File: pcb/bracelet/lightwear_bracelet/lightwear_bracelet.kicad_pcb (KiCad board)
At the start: 2 copper layers, 31 x 20 mm, 20 parts, among them Q1 NMOS, SW1 SW_SPST, U1 ATtiny1616-M, U2 TP4054

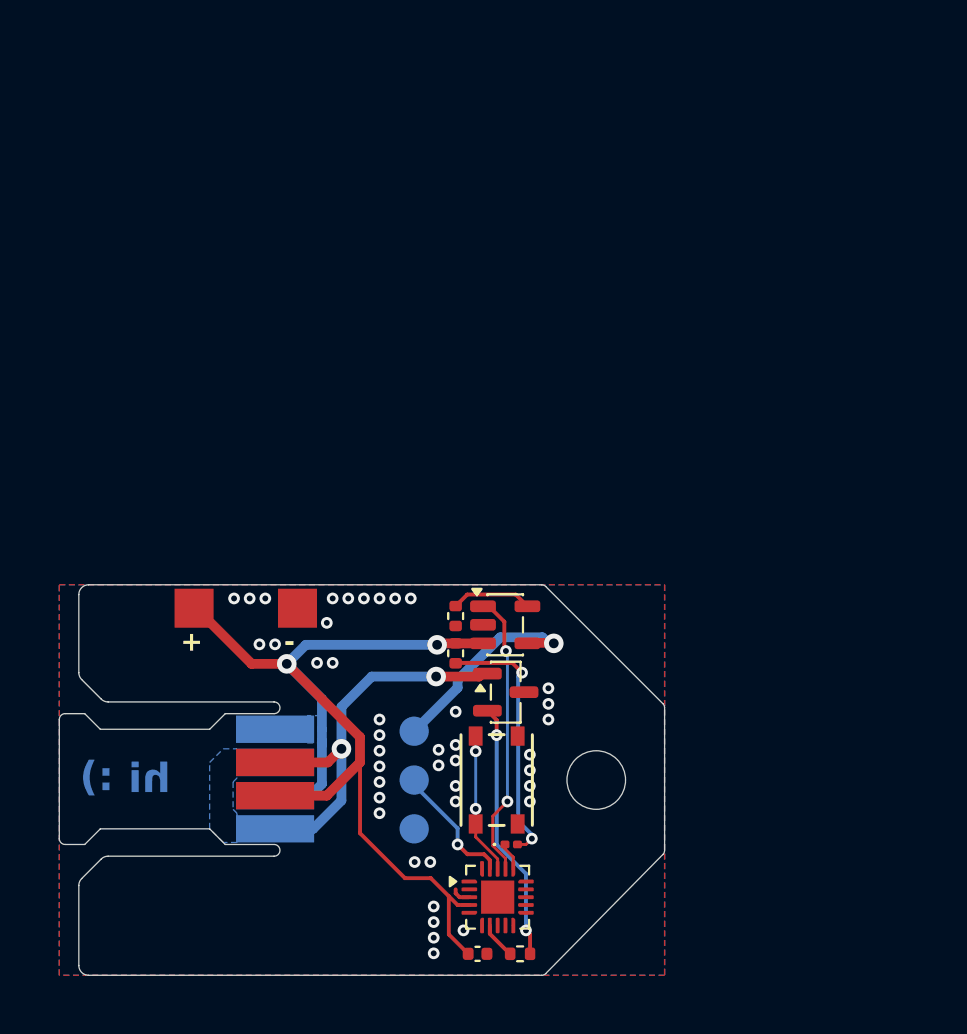
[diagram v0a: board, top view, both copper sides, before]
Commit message: Started work on PCB without battery chips
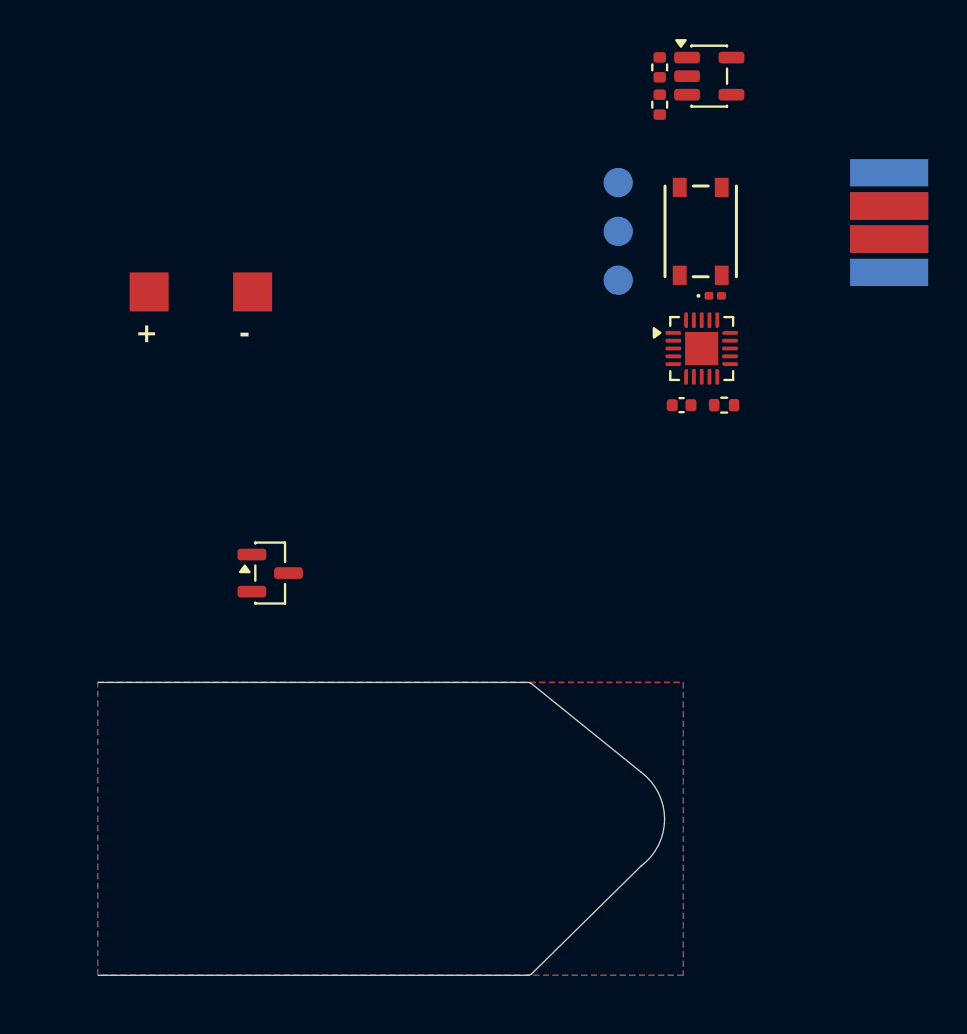
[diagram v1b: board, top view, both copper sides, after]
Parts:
- moved TP10 42.4 mm to (170.5, 58.9)
- moved TP5 42.4 mm to (170.5, 62.3)
- moved TP8 42.4 mm to (170.5, 62.3)
- moved TP9 42.4 mm to (170.5, 64.0)
- moved TP11 42.4 mm to (170.5, 60.6)
- moved TP4 42.4 mm to (170.5, 60.6)
- moved C1 30.0 mm to (159.9, 70.8)
- moved R3 30.0 mm to (162.1, 70.8)
- moved D1 30.0 mm to (161.6, 65.2)
- moved R1 30.0 mm to (158.8, 55.4)
- moved U1 30.0 mm to (160.9, 67.9)
- moved SW1 30.0 mm to (160.8, 61.9)
- moved TP1 30.0 mm to (156.6, 59.4)
- moved TP2 30.0 mm to (156.6, 61.9)
- moved R2 30.0 mm to (158.8, 53.5)
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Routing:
- net +BATT: track 51.7 -> 0.00 mm, vias 2 -> 0
- net /LEDK: track 20.3 -> 0.00 mm, vias 2 -> 0
- net /nCHRG: track 14.9 -> 0.00 mm, vias 2 -> 0
- net Net-(Q1-G): track 13.8 -> 0.00 mm, vias 2 -> 0
- net Net-(D1-A): track 13.5 -> 0.00 mm, vias 2 -> 0
- net +5V: track 10.9 -> 0.00 mm, vias 1 -> 0
- net Net-(SW1-A): track 7.27 -> 0.00 mm, vias 2 -> 0
- net /UPDI: track 6.65 -> 0.00 mm, vias 1 -> 0
- net Net-(U2-PROG): track 4.17 -> 0.00 mm
- net Net-(U1-PA6): track 1.89 -> 0.00 mm
- net Net-(D1-K): track 1.43 -> 0.00 mm
- net GND: track 0.98 -> 0.00 mm, vias 42 -> 0
- removed copper zone on B.Cu, net +BATT
- removed copper zone on B.Cu, net /LEDK
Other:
- board size 31 x 20 mm -> 29 x 15 mm
- board text removed: ":)"
- board text removed: "Stiffener: Polyimide Thickness: 0.15mm Location: Filled zones on this layer, back side of PCB"
- board text removed: "hi"

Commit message: 15x20mm battery version done
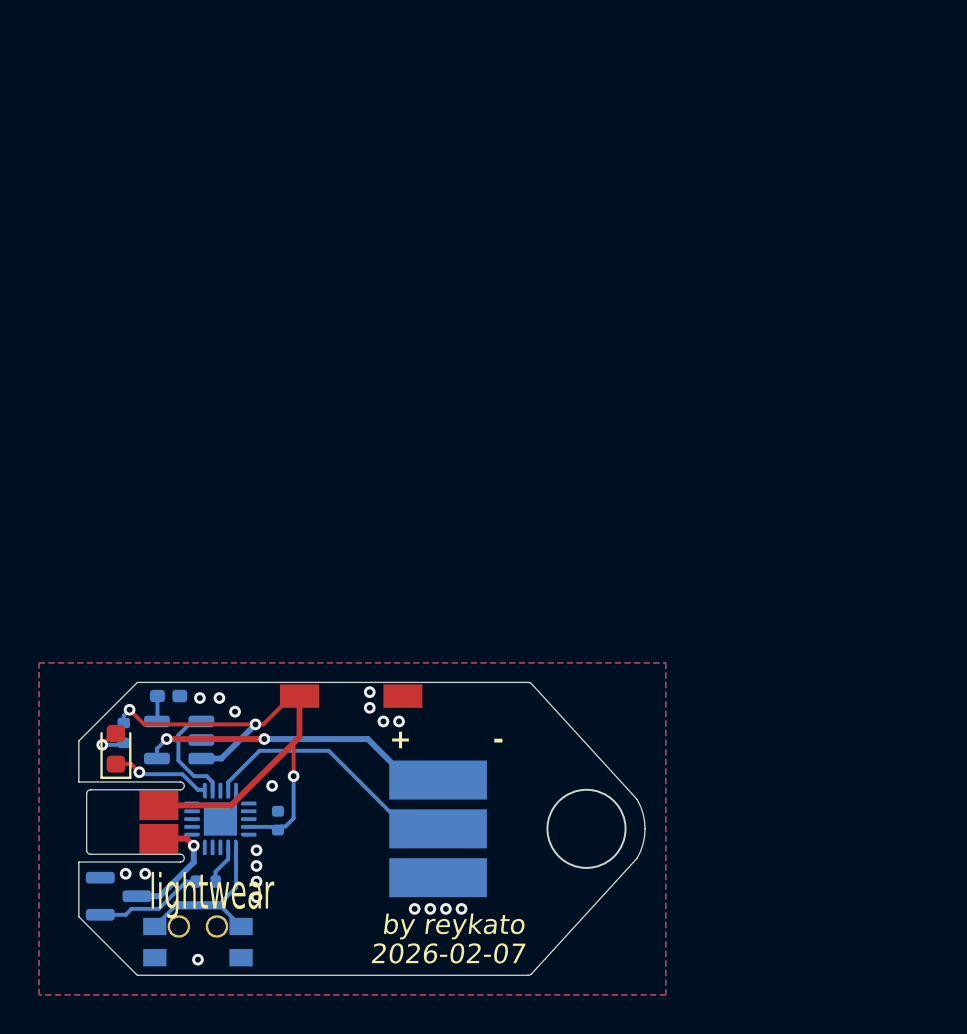
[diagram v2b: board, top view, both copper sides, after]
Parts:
- removed TP10, TP8: LEDA, footprints:TestPoint_Pad_4.0x1.4mm
- removed TP11, TP9: LEDK, footprints:TestPoint_Pad_4.0x1.4mm
- C1, R1, U1, U2: moved to B.Cu
- D1: footprint LED_SMD:LED_0201_0603Metric -> LED_SMD:LED_0603_1608Metric
- Q1: footprint Package_TO_SOT_SMD:SOT-23 -> footprints:SOT-23-MOSFET; moved to B.Cu
- R2: footprint Resistor_SMD:R_0402_1005Metric -> LED_SMD:LED_0402_1005Metric_Pad0.77x0.64mm_HandSolder; moved to B.Cu
- R3: value TBD -> 33R; moved to B.Cu
- SW1: footprint footprints:SW4_PTS815 SJM 250 SMTR LFS_CNK -> footprints:SMT_231GPLFS; moved to B.Cu
- TP1, TP2, TP3: footprint TestPoint:TestPoint_Pad_D1.5mm -> footprints:TestPoint_Pad_5.0x2mm_slim
- TP4, TP5: footprint footprints:TestPoint_Pad_4.0x1.4mm -> footprints:TestPoint_Pad_2.0x1.5mm_slim
- TP6, TP7: footprint footprints:TestPoint_Pad_2.0x2.0mm_slim -> footprints:TestPoint_Pad_2.0x1.2mm_slim
- moved TP4 49.5 mm to (133.1, 93.0), turned to 180 degrees
- moved TP5 47.3 mm to (133.1, 91.3), turned to 180 degrees
- moved SW1 44.6 mm to (135.1, 98.3), turned to 0 degrees
- moved U2 43.5 mm to (134.1, 88.0), turned to 180 degrees
- moved R1 42.3 mm to (131.3, 87.6)
- moved R2 40.9 mm to (133.6, 85.7), turned to 0 degrees
- moved D1 38.5 mm to (130.9, 88.4), turned to 90 degrees
- moved R3 36.1 mm to (135.5, 95.2), turned to 180 degrees
- moved U1 34.5 mm to (136.2, 92.0), turned to 180 degrees
- moved TP1 32.0 mm to (147.4, 90.0), turned to 0 degrees
- moved TP2 32.0 mm to (147.4, 92.5), turned to 0 degrees
- moved TP3 32.0 mm to (147.4, 95.0), turned to 0 degrees
- moved C1 29.7 mm to (139.2, 92.1), turned to 90 degrees
- moved TP6 22.1 mm to (140.3, 85.7)
- moved TP7 22.1 mm to (145.6, 85.7)
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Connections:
- SW1 pad 1: Net-(SW1-A) -> GND
- SW1 pad 2: GND -> Net-(SW1-B)
- U1 pad 18: Net-(SW1-A) -> unconnected-(U1-PC3-Pad18)
- U1 pad 6: unconnected-(U1-PA5-Pad6) -> Net-(SW1-B)
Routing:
- net +BATT: track 0.00 -> 32.0 mm, vias 0 -> 3
- net +5V: track 0.00 -> 16.0 mm, vias 0 -> 2
- net /UPDI: track 0.00 -> 13.5 mm
- net Net-(SW1-B): track 0.00 -> 9.70 mm
- net /LEDK: track 0.00 -> 6.42 mm, vias 0 -> 1
- net Net-(Q1-G): track 0.00 -> 5.59 mm
- net /nCHRG: track 0.00 -> 5.41 mm
- net Net-(D1-K): track 0.00 -> 5.11 mm, vias 0 -> 1
- net Net-(D1-A): track 0.00 -> 2.08 mm, vias 0 -> 1
- net Net-(U1-PA6): track 0.00 -> 2.02 mm
- net Net-(U2-PROG): track 0.00 -> 1.31 mm
- net GND: vias 0 -> 19
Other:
- outline, holes or cut-outs redrawn
- board text added: "2026-02-07"
- board text removed: "2025-12-23"
- board text removed: "rev 0"

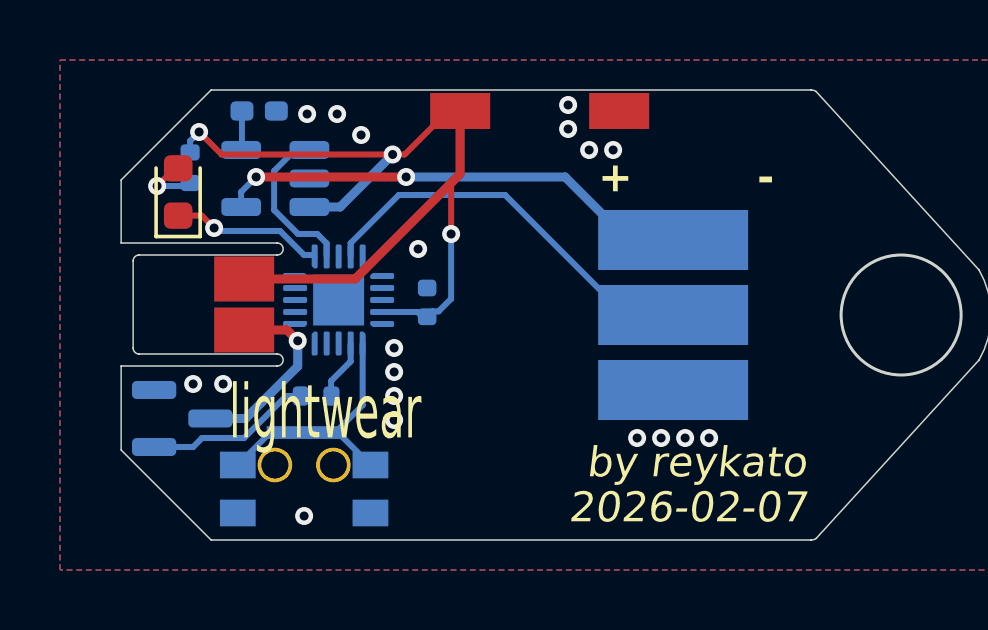
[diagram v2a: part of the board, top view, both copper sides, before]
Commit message: code for bracelet working. 4 brightness modes (including OFF) and battery checking (25% increments)
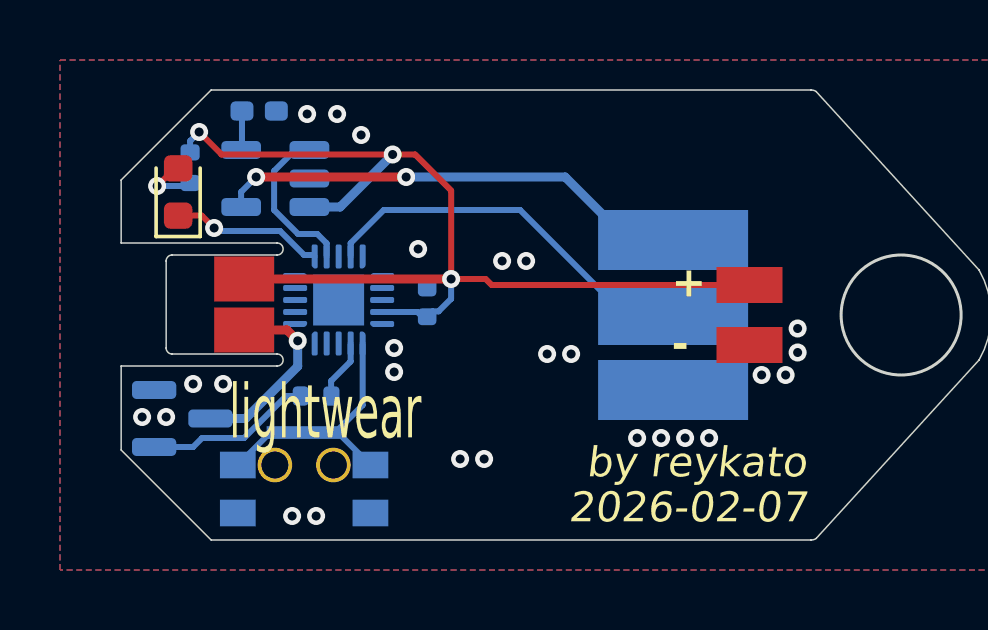
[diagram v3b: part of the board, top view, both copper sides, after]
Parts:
- removed TP7: -BATT, footprints:TestPoint_Pad_2.0x1.2mm_slim
- TP6: value +BATT -> TestPoint_2Pole; footprint footprints:TestPoint_Pad_2.0x1.2mm_slim -> footprints:BatteryBMSBoardPads
- moved TP6 11.8 mm to (149.9, 92.5)
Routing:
- net +BATT: track 32.0 -> 36.7 mm
- net GND: vias 19 -> 26
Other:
- outline, holes or cut-outs redrawn
- board text removed: "+"
- board text removed: "-"
